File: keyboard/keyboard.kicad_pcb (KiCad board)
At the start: 2 copper layers, 117 parts, among them J1 USB_C_Receptacle_USB2.0_16P, SW1 Keyswitch, SW10 Keyswitch, SW11 Keyswitch, SW12 Keyswitch, SW13 Keyswitch, SW14 Keyswitch, SW15 Keyswitch, SW16 Keyswitch, SW17 Keyswitch, SW18 Keyswitch, SW19 Keyswitch, SW2 Keyswitch, SW20 Keyswitch, SW21 Keyswitch, SW22 Keyswitch, SW23 Keyswitch, SW24 Keyswitch, SW25 Keyswitch, SW26 Keyswitch, SW27 Keyswitch, SW29 Keyswitch, SW3 Keyswitch, SW31 Keyswitch, SW32 Keyswitch, SW33 Keyswitch, SW34 Keyswitch, SW35 Keyswitch, SW36 Keyswitch, SW37 Keyswitch, SW38 Keyswitch, SW39 Keyswitch, SW4 Keyswitch, SW40 Keyswitch, SW41 Keyswitch, SW42 Keyswitch, SW43 Keyswitch, SW44 Keyswitch, SW45 Keyswitch, SW46 Keyswitch, SW47 Keyswitch, SW48 Keyswitch, SW49 SW_SPDT, SW5 Keyswitch, SW50 SW_Push, SW6 Keyswitch, SW7 Keyswitch, SW8 Keyswitch, SW9 Keyswitch, U1 USBLC6-2P6, U2 STM32F072CBU7, U3 AP2112K-3.3

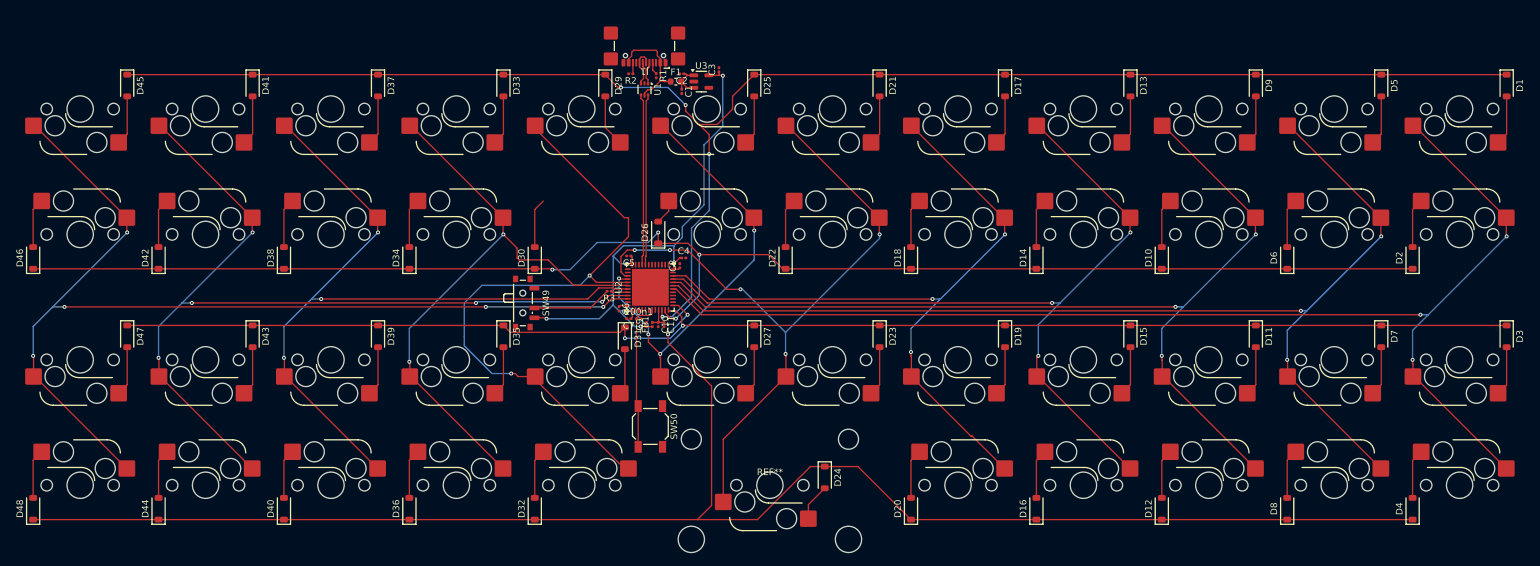
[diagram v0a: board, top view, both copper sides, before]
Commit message: feat(keyboard): finish route, edges and silk
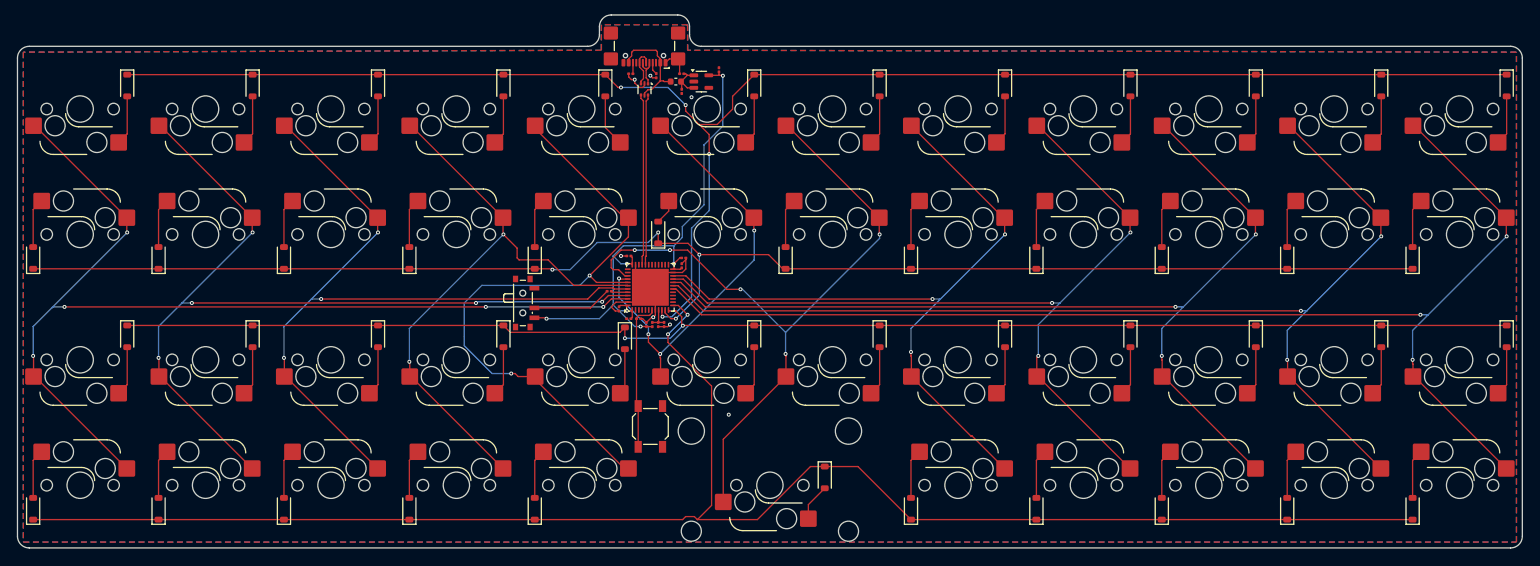
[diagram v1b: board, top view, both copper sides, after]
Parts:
- added SW30: Keyswitch, PCM_Switch_Keyboard_Hotswap_Kailh:SW_Hotswap_Kailh_MX, B.Cu at (118.1, 52.1)
- SW1, SW10, SW11, SW12, SW13, SW14, SW15, SW16, SW17, SW18, SW19, SW2, SW20, SW21, SW22, SW23, SW25, SW26, SW27, SW29, SW3, SW31, SW32, SW33, SW34, SW35, SW36, SW37, SW38, SW39, SW4, SW40, SW41, SW42, SW43, SW44, SW45, SW46, SW47, SW48, SW5, SW6, SW7, SW8, SW9: footprint PCM_Switch_Keyboard_Hotswap_Kailh:SW_Hotswap_Kailh_MX_1.00u -> PCM_Switch_Keyboard_Hotswap_Kailh:SW_Hotswap_Kailh_MX
- SW24: footprint PCM_Switch_Keyboard_Hotswap_Kailh:SW_Hotswap_Kailh_MX_2.00u -> PCM_Switch_Keyboard_Hotswap_Kailh:SW_Hotswap_Kailh_MX
- moved C8 0.30 mm to (133.3, 56.9)
- turned REF** to 180 degrees
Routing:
- net GND: track 0.00 -> 42.4 mm, vias 0 -> 7
- net Col 5: track 107.3 -> 109.5 mm
- added copper zone on B.Cu, net GND
- added copper zone on F.Cu, net GND
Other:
- board outline added: 228.6 x 81 mm

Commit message: feat(keyboard): fix bom and cpl
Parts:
- C0: renamed from 100n1; value C0 -> 100n; footprint Capacitor_SMD:C_0201_0603Metric -> Capacitor_SMD:C_0603_1608Metric
- C1, C10, C11, C2, C3, C4, C5, C6, C7, C8, C9: footprint Capacitor_SMD:C_0201_0603Metric -> Capacitor_SMD:C_0603_1608Metric
- FB1: footprint Inductor_SMD:L_0201_0603Metric -> Inductor_SMD:L_0603_1608Metric
- J1: footprint Connector_USB:USB_C_Receptacle_GCT_USB4110 -> Connector_USB:USB_C_Receptacle_XKB_U262-16XN-4BVC11
- R1, R2, R3: footprint Resistor_SMD:R_0201_0603Metric -> Resistor_SMD:R_0603_1608Metric
- moved C0 11.2 mm to (128.8, 75.9)
- moved C1 5.62 mm to (136.3, 25.6), turned to 90 degrees
- moved R3 5.06 mm to (117.8, 63.1)
- moved D35 4.18 mm to (106.5, 71.8)
- moved D31 3.97 mm to (125.6, 71.8)
- moved C6 3.47 mm to (125.6, 66.4)
- moved C2 2.56 mm to (134.8, 25.6), turned to 90 degrees
- moved C7 2.10 mm to (123.2, 64.6), turned to -90 degrees
- moved C3 1.91 mm to (137.8, 25.6)
- moved C11 1.07 mm to (131.5, 66.4)
- moved C9 1.07 mm to (127.0, 66.4)
- moved C8 0.94 mm to (134.2, 57.2), turned to 0 degrees
- moved C5 0.89 mm to (125.3, 54.5), turned to 90 degrees
- moved R2 0.89 mm to (125.6, 28.6), turned to -90 degrees
- moved R1 0.67 mm to (129.7, 28.6)
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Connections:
- U2 pad 10: Row 0 -> unconnected-(U2-PA0-Pad10)
- U2 pad 11: Row 1 -> unconnected-(U2-PA1-Pad11)
- U2 pad 12: Row 2 -> Row 3
- U2 pad 13: Row 3 -> Row 2
- U2 pad 14: unconnected-(U2-PA4-Pad14) -> Row 1
- U2 pad 15: unconnected-(U2-PA5-Pad15) -> Row 0
- U2 pad 16: unconnected-(U2-PA6-Pad16) -> Col 0
- U2 pad 17: unconnected-(U2-PA7-Pad17) -> Col 1
- U2 pad 18: Col 0 -> Col 2
- U2 pad 19: Col 1 -> Col 3
- U2 pad 20: Col 2 -> Col 4
- U2 pad 21: Col 3 -> Col 5
- U2 pad 22: Col 4 -> Col 6
- U2 pad 39: Col 5 -> unconnected-(U2-PB3-Pad39)
- U2 pad 40: Col 6 -> unconnected-(U2-PB4-Pad40)
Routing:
- net Col 7: track 97.8 -> 74.5 mm
- net Col 5: track 109.5 -> 96.8 mm, vias 5 -> 3
- net Row 2: track 216.6 -> 227.9 mm, vias 2 -> 4
- net GND: track 42.4 -> 32.0 mm, vias 7 -> 4
- net Col 6: track 65.5 -> 58.6 mm, vias 4 -> 3
- net Col 8: track 93.0 -> 99.3 mm, vias 2 -> 3
- net Net-(SW49-B): track 12.1 -> 5.92 mm
- net BOOT: track 2.56 -> 7.38 mm
- net +3V3: track 86.3 -> 81.7 mm, vias 6 -> 5
- net Net-(D35-A): track 7.54 -> 3.50 mm
- net Col 10: track 138.2 -> 142.1 mm, vias 5 -> 3
- net Col 11: track 158.1 -> 162.0 mm, vias 5 -> 3
- net Net-(D31-A): track 7.00 -> 3.50 mm
- net Row 3: track 255.4 -> 257.2 mm, vias 2 -> 0
- net VBUS: track 6.51 -> 8.01 mm
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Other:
- board size 228.6 x 81 mm -> 228.6 x 79.8 mm

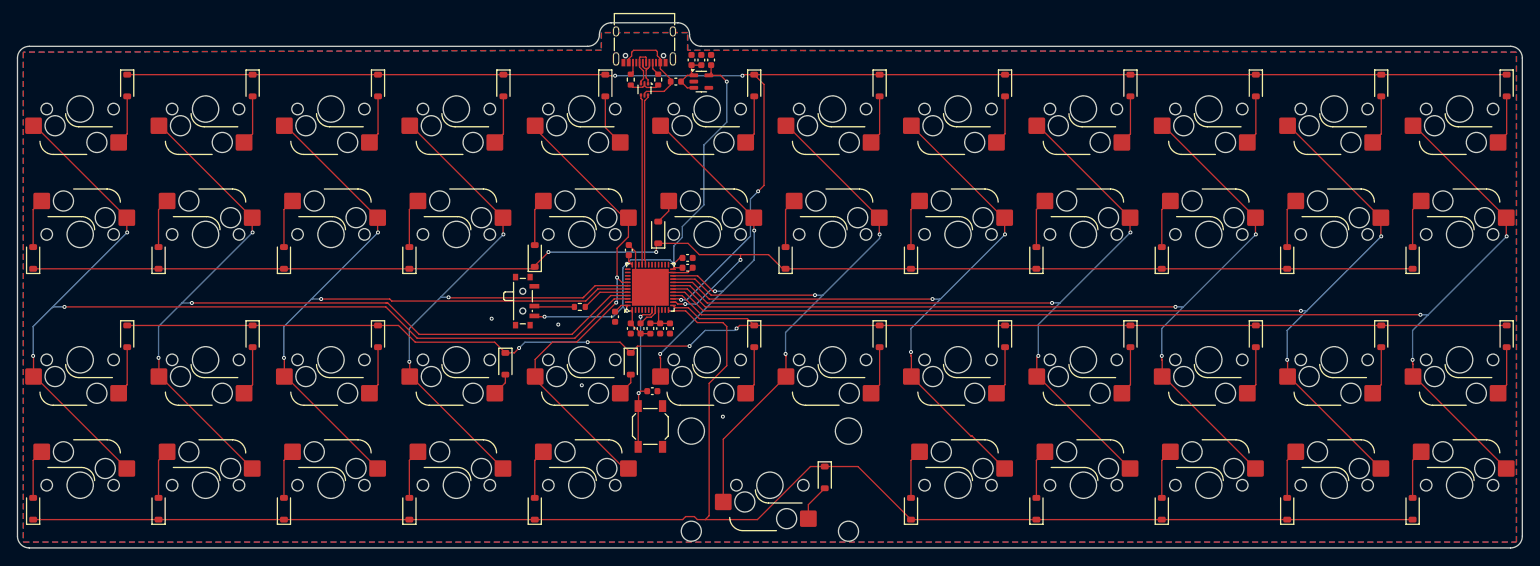
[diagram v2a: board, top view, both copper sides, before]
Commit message: feat(keyboard): changed from QFP48 to LQFP48
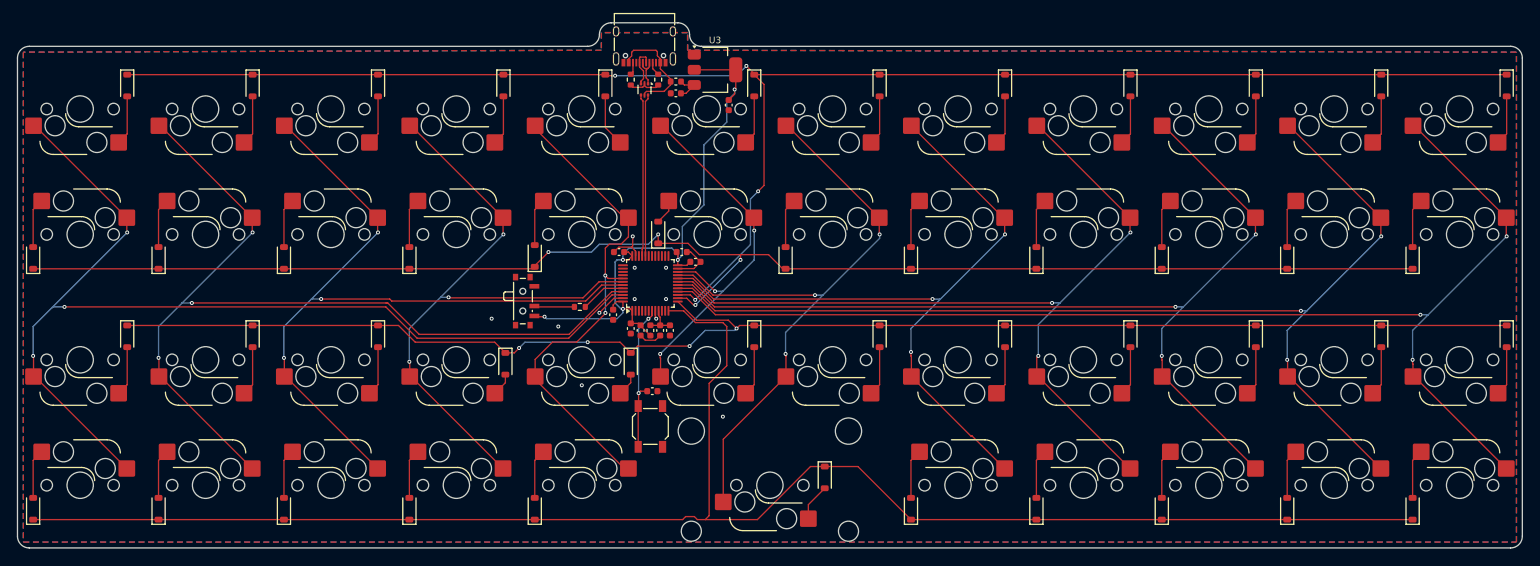
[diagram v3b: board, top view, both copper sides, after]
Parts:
- removed C2: 100n, Capacitor_SMD:C_0603_1608Metric
- C1: value 1u -> 10u
- C3: value 1u -> 22u
- U2: value STM32F072CBU7 -> STM32F072CBT6; footprint Package_DFN_QFN:QFN-48-1EP_7x7mm_P0.5mm_EP5.6x5.6mm -> Package_QFP:LQFP-48_7x7mm_P0.5mm
- U3: value AP2112K-3.3 -> AMS1117-3.3; footprint Package_TO_SOT_SMD:SOT-23-5 -> Package_TO_SOT_SMD:SOT-223-3_TabPin2
- moved C3 7.35 mm to (140.4, 32.5), turned to -90 degrees
- moved C1 6.37 mm to (132.4, 30.7), turned to 180 degrees
- moved U3 2.74 mm to (138.4, 27.1)
- moved C5 1.52 mm to (123.8, 54.8), turned to 180 degrees
- moved C8 1.49 mm to (135.4, 56.3)
- moved C4 1.26 mm to (133.3, 54.8)
- moved U2 0.60 mm to (128.5, 59.6)
- moved C7 0.42 mm to (122.9, 64.3)
- moved C10 0.30 mm to (130.0, 66.7)
- moved C11 0.30 mm to (131.5, 66.7)
- moved C9 0.30 mm to (127.0, 66.7), turned to -90 degrees
- moved FB1 0.30 mm to (128.5, 66.7)
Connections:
- U3 pad 1: VBUS -> GND
- U3 pad 2: GND -> +3V3
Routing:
- net +3V3: track 81.7 -> 94.3 mm
- net GND: track 32.0 -> 27.2 mm, vias 4 -> 11
- net VBUS: track 8.01 -> 4.78 mm
- net Row 2: track 227.9 -> 225.0 mm
- net Col 7: track 74.5 -> 76.5 mm
- net D-: track 26.1 -> 24.6 mm
- net Row 0: track 251.5 -> 253.0 mm
- net Row 1: track 227.6 -> 228.9 mm
- net D+: track 25.9 -> 24.6 mm
- net RST: track 23.8 -> 23.0 mm
- net VDDA: track 5.12 -> 5.69 mm
- net Col 8: track 99.3 -> 98.8 mm
